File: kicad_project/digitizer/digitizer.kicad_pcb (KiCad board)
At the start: 2 copper layers, 96 x 74 mm, 63 parts, among them IC201 MAX3059ASA+T UPSTREAM, IC202 MAX6035AAUR50+T, IC203 MAX3059ASA+T DOWNSTREAM, IC204 MAX6043BAUT33+T, IC301 ADS1234IPWR, J201 DT15-4P (UPSTREAM), J202 DT06-4S (DOWNSTREAM), J301 Load Cell 1, J302 Load Cell 2, J303 Load Cell 3, J401 SHF-105-01-L-D-TH-TR, U401 ATSAM4E8EA-AN

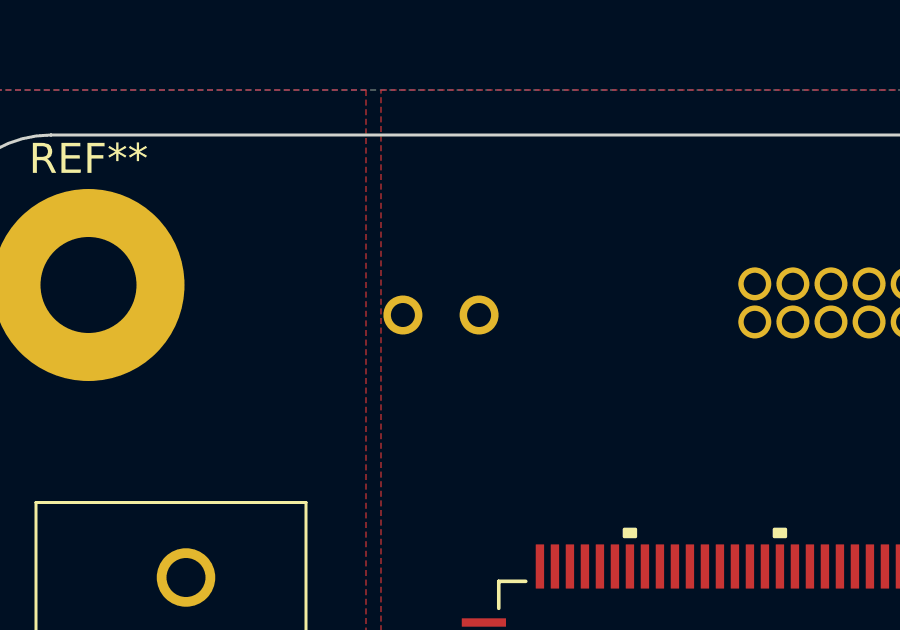
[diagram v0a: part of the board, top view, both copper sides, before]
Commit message: updated copper zones to properly connect to tiny solder pads
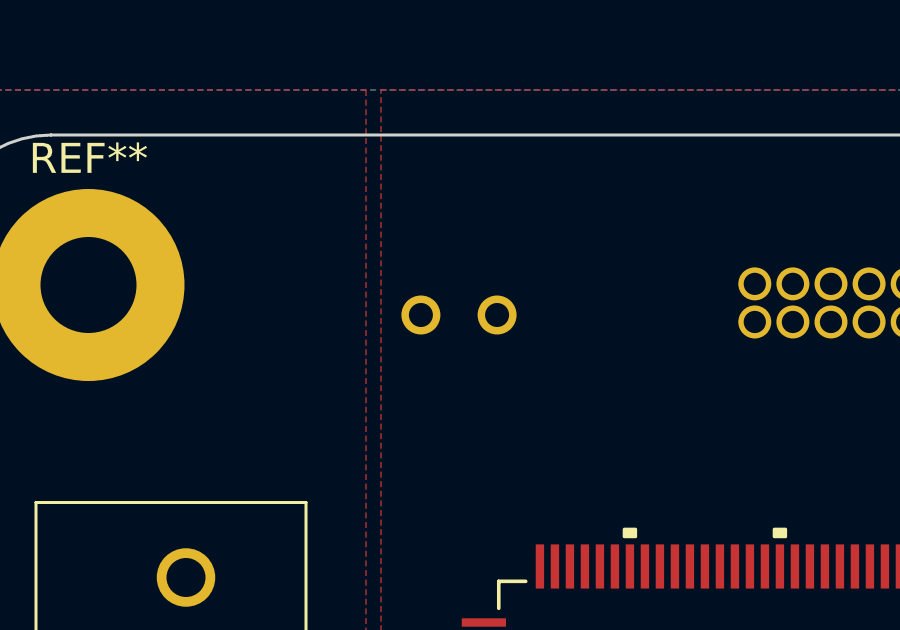
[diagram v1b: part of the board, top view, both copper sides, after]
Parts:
- moved LED201 0.60 mm to (91.6, 55.0)
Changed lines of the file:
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@@
   )
   (footprint "SamacSys_Parts:HLMPY802F0000" (layer "B.Cu")
-    (at 91 55 180)
+    (at 91.6 55 180)
     (descr "HLMP-Y802-F0000-1")
     (tags "LED")
@@
   (gr_arc (start 166.5 49) (mid 169.15165 50.09835) (end 170.25 52.75) (layer "Edge.Cuts") (width 0.1))
   (zone (net 3) (net_name "3V3_CLEAN") (layer "F.Cu") (name "3V3_CLEAN_PLANE") (hatch edge 0.508)
-    (connect_pads (clearance 0.508))
-    (min_thickness 0.254) (filled_areas_thickness no)
+    (connect_pads (clearance 0.254))
+    (min_thickness 0.127) (filled_areas_thickness no)
     (fill yes (thermal_gap 0.508) (thermal_bridge_width 0.508))
     (polygon
@@
   )
   (zone (net 2) (net_name "5V_CLEAN") (layer "F.Cu") (name "5V)CLEAN_PLANE") (hatch edge 0.508)
-    (connect_pads (clearance 0.508))
-    (min_thickness 0.254) (filled_areas_thickness no)
+    (connect_pads (clearance 0.254))
+    (min_thickness 0.127) (filled_areas_thickness no)
     (fill yes (thermal_gap 0.508) (thermal_bridge_width 0.508))
     (polygon

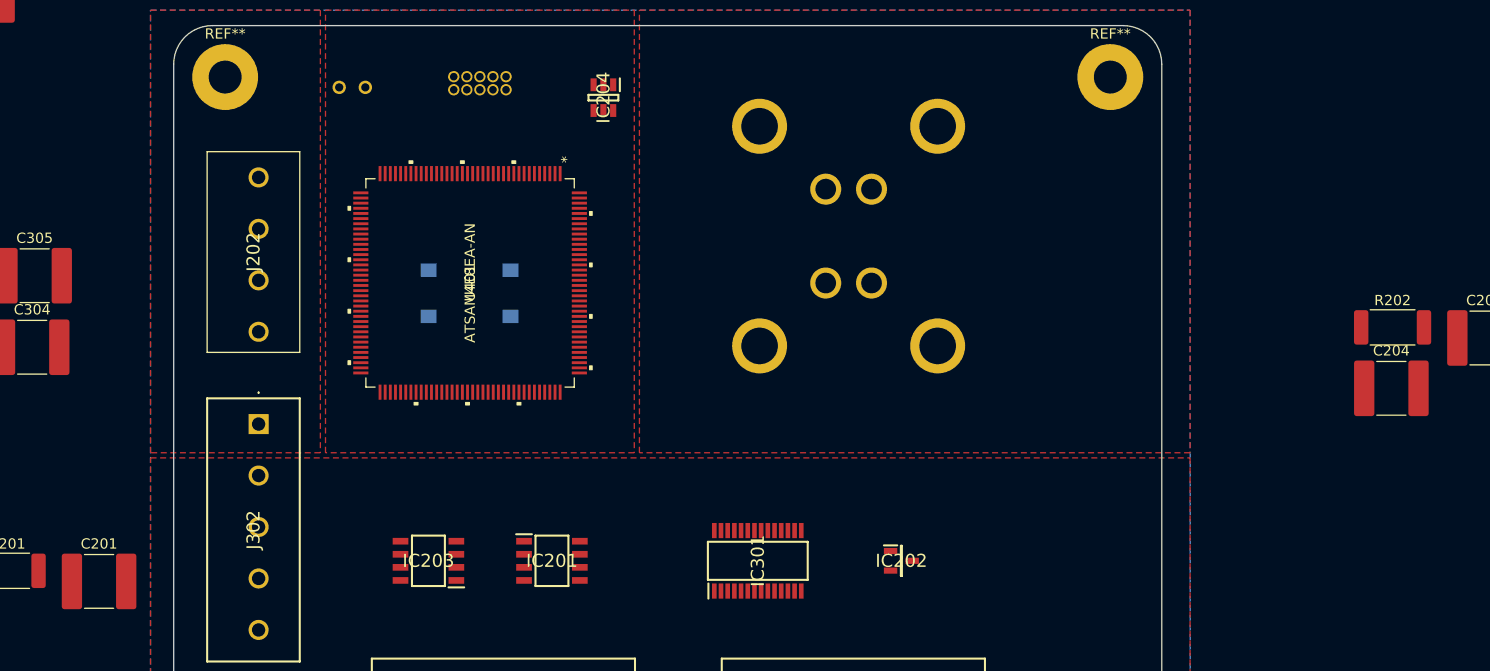
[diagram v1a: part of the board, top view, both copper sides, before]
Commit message: placed & routed bypass capacitors for both power regulators
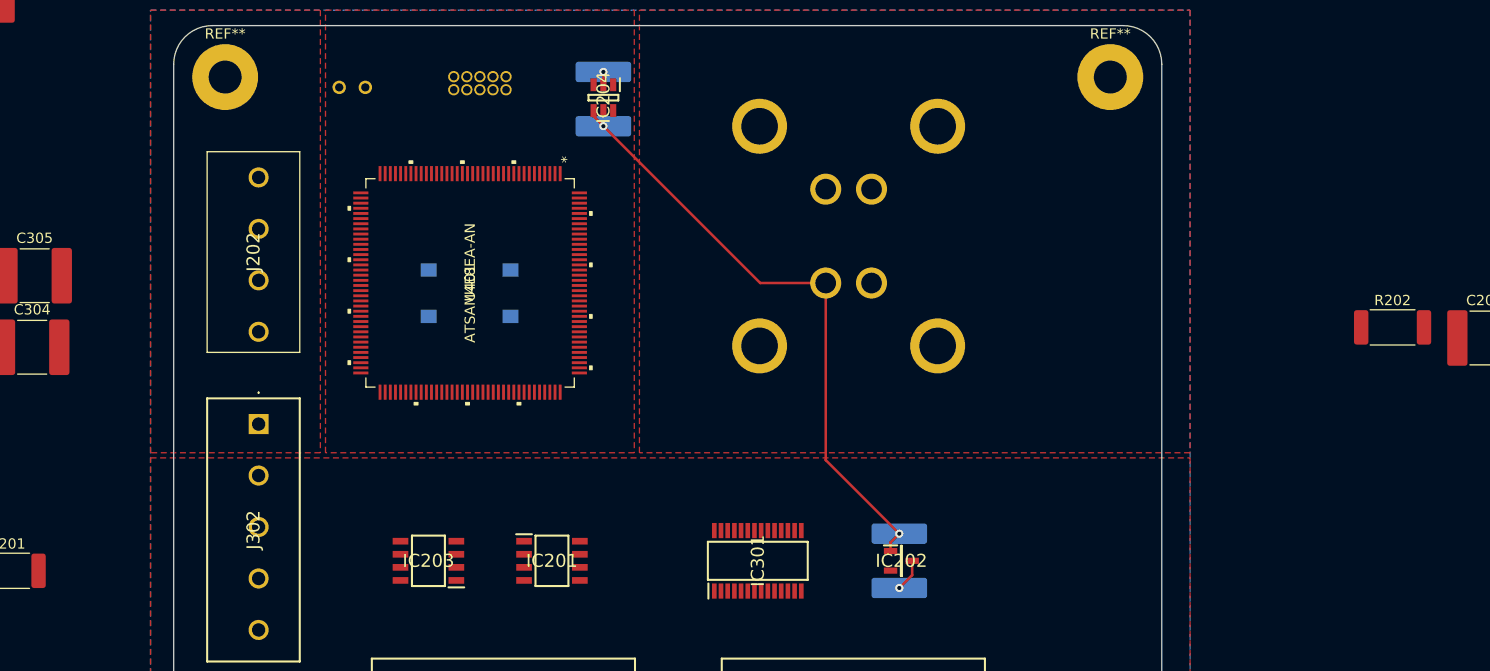
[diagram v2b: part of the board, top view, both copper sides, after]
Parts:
- C201, C204: moved to B.Cu
- moved C204 81.6 mm to (116.0, 56.1), turned to 90 degrees
- moved C201 77.8 mm to (144.8, 101.0), turned to -90 degrees
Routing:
- net 12V_CLEAN: track 0.00 -> 59.2 mm, vias 0 -> 2
- net GND: track 0.00 -> 4.41 mm, vias 0 -> 2

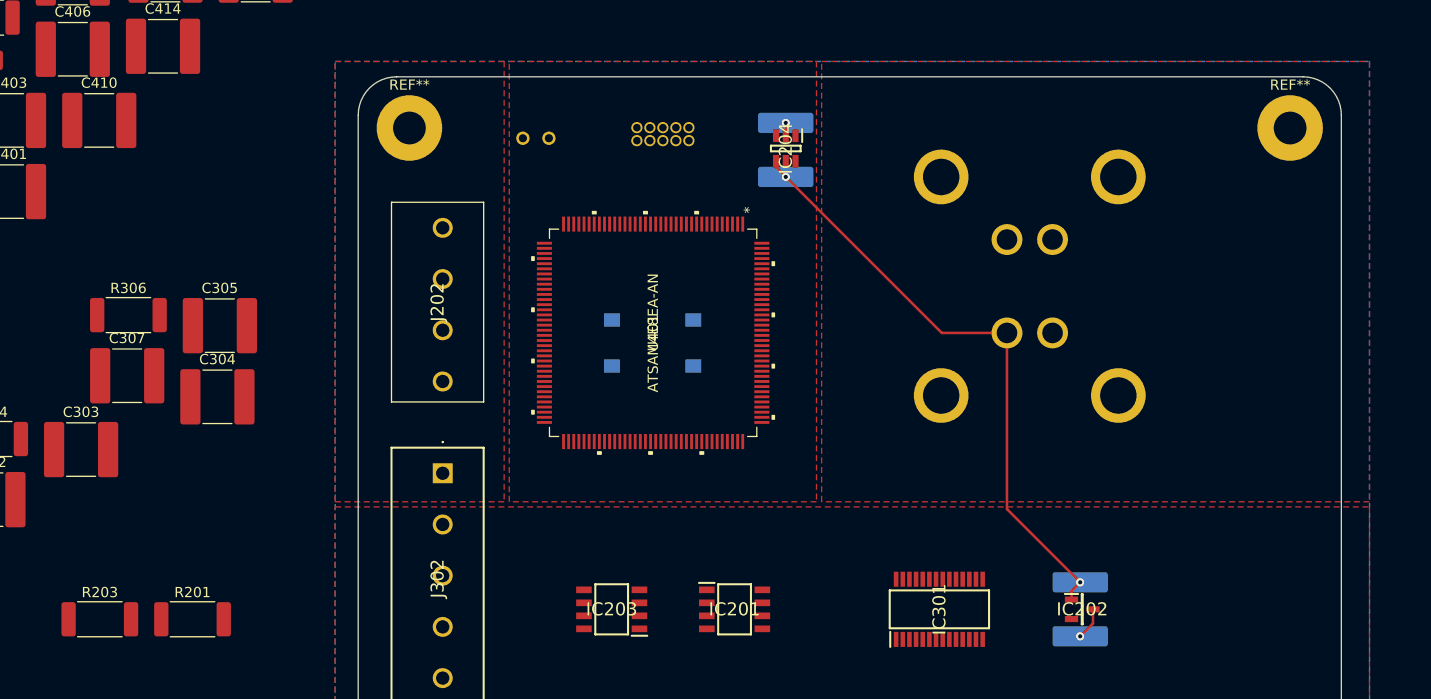
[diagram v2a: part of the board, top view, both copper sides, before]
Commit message: routed LED connections; replaced 12V_CLEAN copper zone so it was one consecutive zone instead of 2 separate zones
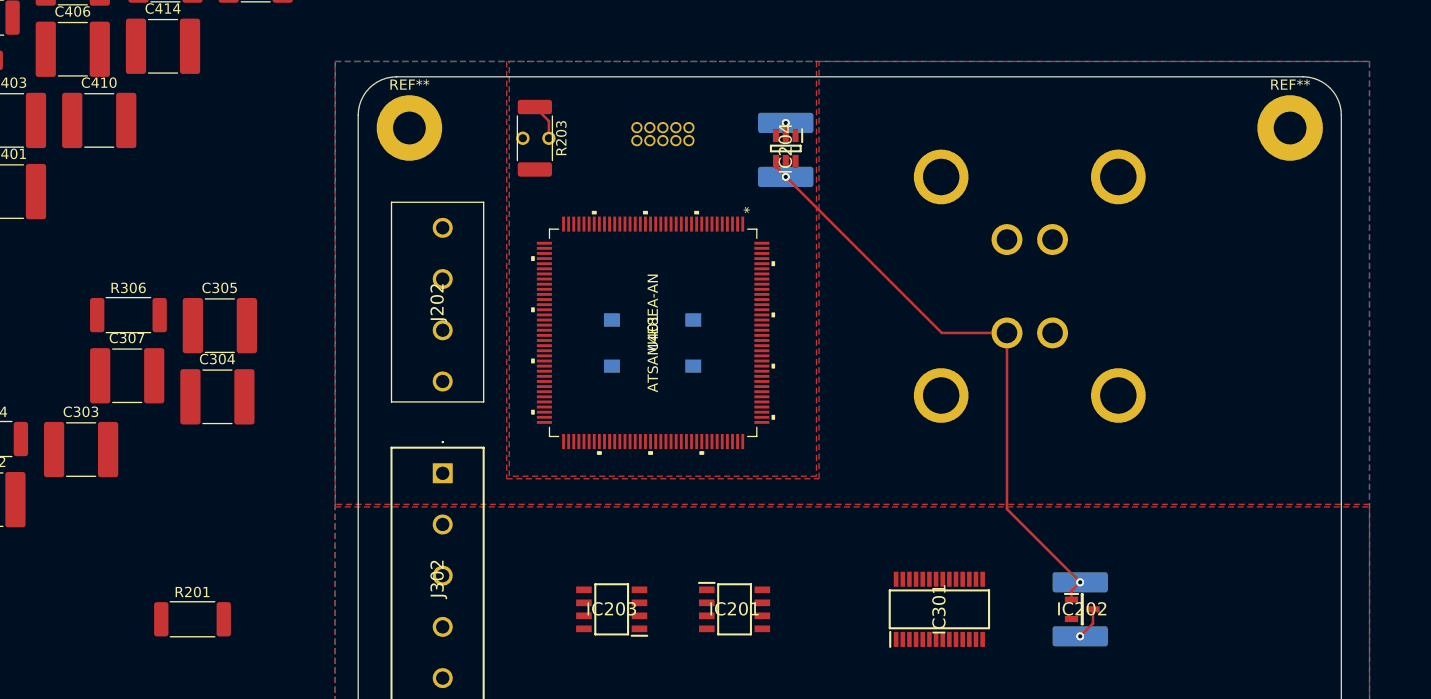
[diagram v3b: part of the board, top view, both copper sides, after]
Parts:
- moved R203 63.3 mm to (91.5, 55.0), turned to -90 degrees
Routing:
- net Net-(LED201-Pad1): track 0.00 -> 3.62 mm
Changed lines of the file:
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@@
   )
   (footprint "Resistor_SMD:R_2512_6332Metric_Pad1.40x3.35mm_HandSolder" (layer "F.Cu")
-    (at 49.02 101.97)
+    (at 91.5 55 -90)
     (descr "Resistor SMD 2512 (6332 Metric), square (rectangular) end terminal, IPC_7351 nominal with elongated pad for handsoldering. (Body size source: IPC-SM-782 page 72, https://www.pcb-3d.com/wordpress/wp-content/uploads/ipc-sm-782a_amendment_1_and_2.pdf), generated with kicad-footprint-generator")
     (tags "resistor handsolder")
@@
     (property "Sheetname" "CANPWR")
     (attr smd)
-    (fp_text reference "R203" (at 0 -2.62) (layer "F.SilkS")
-      (effects (font (size 1 1) (thickness 0.15)))
-    )
-    (fp_text value "47" (at 0 2.62) (layer "F.Fab")
-      (effects (font (size 1 1) (thickness 0.15)))
-    )
-    (fp_text user "${REFERENCE}" (at 0 0) (layer "F.Fab")
+    (fp_text reference "R203" (at 0 -2.62 90) (layer "F.SilkS")
+      (effects (font (size 1 1) (thickness 0.15)))
+    )
+    (fp_text value "47" (at 0 2.62 90) (layer "F.Fab")
+      (effects (font (size 1 1) (thickness 0.15)))
+    )
+    (fp_text user "${REFERENCE}" (at 0 0 90) (layer "F.Fab")
       (effects (font (size 1 1) (thickness 0.15)))
     )
@@
     (fp_line (start -3.15 1.6) (end -3.15 -1.6) (layer "F.Fab") (width 0.1))
     (fp_line (start -3.15 -1.6) (end 3.15 -1.6) (layer "F.Fab") (width 0.1))
-    (pad "1" smd roundrect locked (at -3.05 0) (size 1.4 3.35) (layers "F.Cu" "F.Paste" "F.Mask") (roundrect_rratio 0.178571)
+    (pad "1" smd roundrect locked (at -3.05 0 270) (size 1.4 3.35) (layers "F.Cu" "F.Paste" "F.Mask") (roundrect_rratio 0.178571)
       (net 37 "Net-(LED201-Pad1)") (pintype "passive"))
-    (pad "2" smd roundrect locked (at 3.05 0) (size 1.4 3.35) (layers "F.Cu" "F.Paste" "F.Mask") (roundrect_rratio 0.178571)
+    (pad "2" smd roundrect locked (at 3.05 0 270) (size 1.4 3.35) (layers "F.Cu" "F.Paste" "F.Mask") (roundrect_rratio 0.178571)
       (net 3 "3V3_CLEAN") (pintype "passive"))
     (model "${KICAD6_3DMODEL_DIR}/Resistor_SMD.3dshapes/R_2512_6332Metric.wrl"
@@
   (via (at 116 53.5) (size 0.8) (drill 0.4) (layers "F.Cu" "B.Cu") (net 1))
   (via (at 144.75 103.6375) (size 0.8) (drill 0.4) (layers "F.Cu" "B.Cu") (net 1))
+  (segment (start 92.87 53.32) (end 91.5 51.95) (width 0.25) (layer "F.Cu") (net 37))
+  (segment (start 92.87 55) (end 92.87 53.32) (width 0.25) (layer "F.Cu") (net 37))
   (segment (start 143.9 100.05) (end 143.9 99.2125) (width 0.25) (layer "F.Cu") (net 149))
   (segment (start 115.05 57.825) (end 116 58.775) (width 0.25) (layer "F.Cu") (net 149))
@@
     (polygon
       (pts
-        (xy 119 90.5)
-        (xy 89 90.5)
+        (xy 119 88)
+        (xy 89 88)
         (xy 89 47.5)
         (xy 119 47.5)
@@
     )
   )
-  (zone (net 149) (net_name "12V_CLEAN") (layer "F.Cu") (name "12V_CLEAN_PLANE_2") (hatch edge 0.508)
-    (connect_pads (clearance 0.508))
-    (min_thickness 0.254) (filled_areas_thickness no)
-    (fill yes (thermal_gap 0.508) (thermal_bridge_width 0.508))
-    (polygon
-      (pts
-        (xy 88.5 90.5)
-        (xy 72 90.5)
-        (xy 72 47.5)
-        (xy 88.5 47.5)
-      )
-    )
-  )
   (zone (net 149) (net_name "12V_CLEAN") (layer "F.Cu") (name "12V_CLEAN_PLANE") (hatch edge 0.508)
     (connect_pads (clearance 0.508))
@@
     (polygon
       (pts
-        (xy 173 90.5)
-        (xy 119.5 90.5)
-        (xy 119.5 47.5)
+        (xy 88.75 88.25)
+        (xy 119.25 88.25)
+        (xy 119.25 47.5)
         (xy 173 47.5)
+        (xy 173 90.75)
+        (xy 72 90.75)
+        (xy 72 47.5)
+        (xy 88.75 47.5)
       )
     )
